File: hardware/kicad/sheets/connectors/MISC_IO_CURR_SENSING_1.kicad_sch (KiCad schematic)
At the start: 20 parts

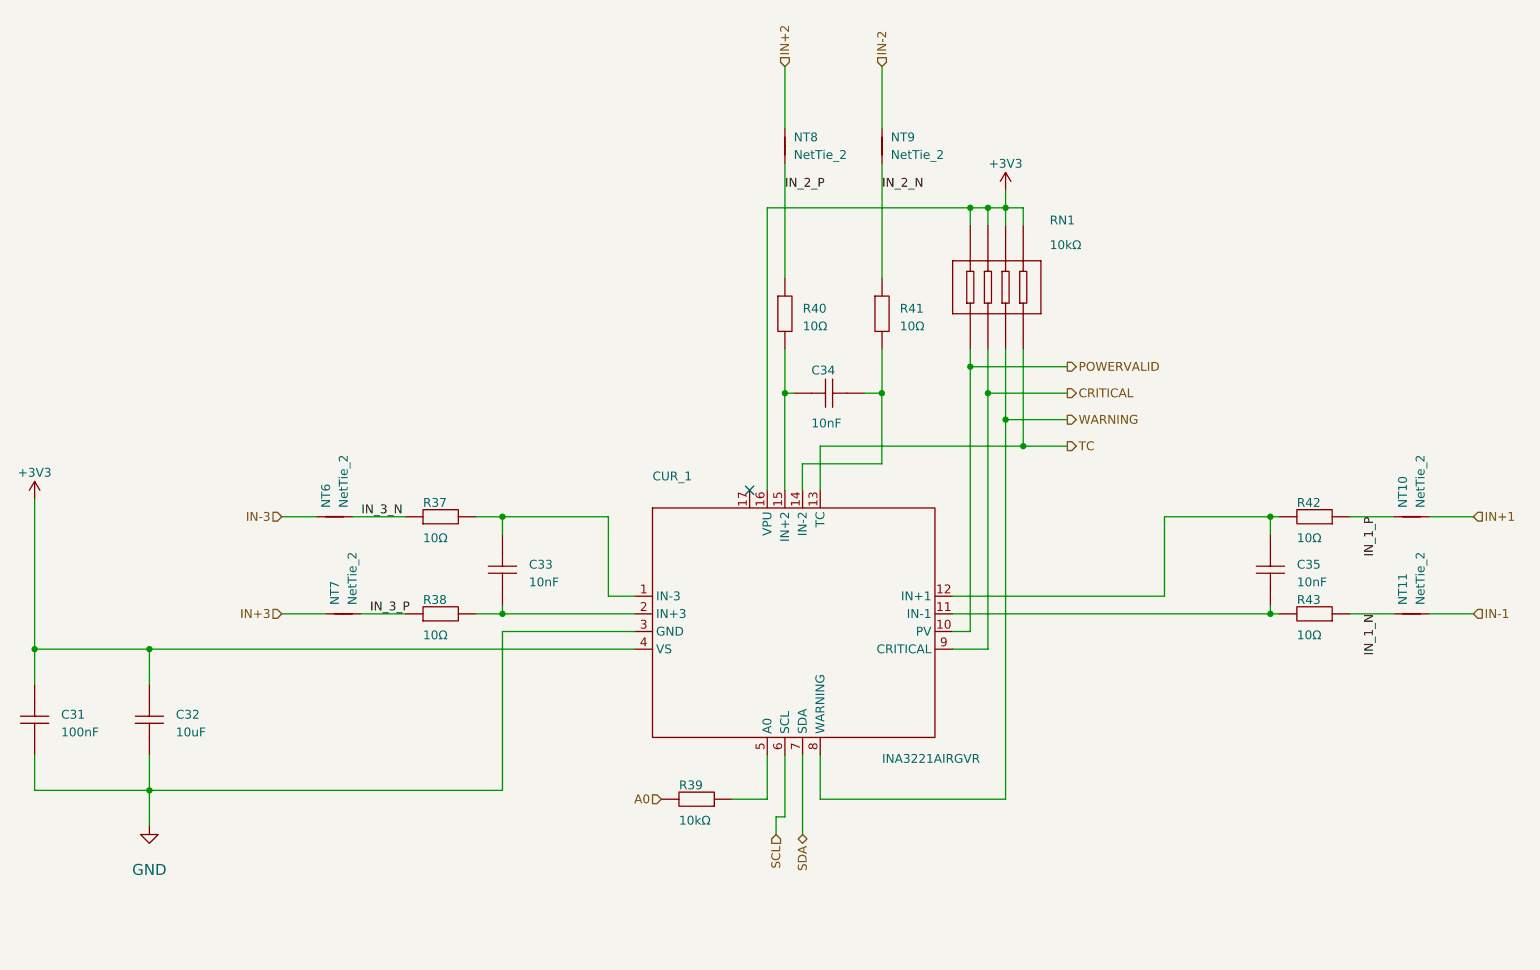
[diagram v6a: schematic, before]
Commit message: current sensing on the servos and cleaning up empty sheets
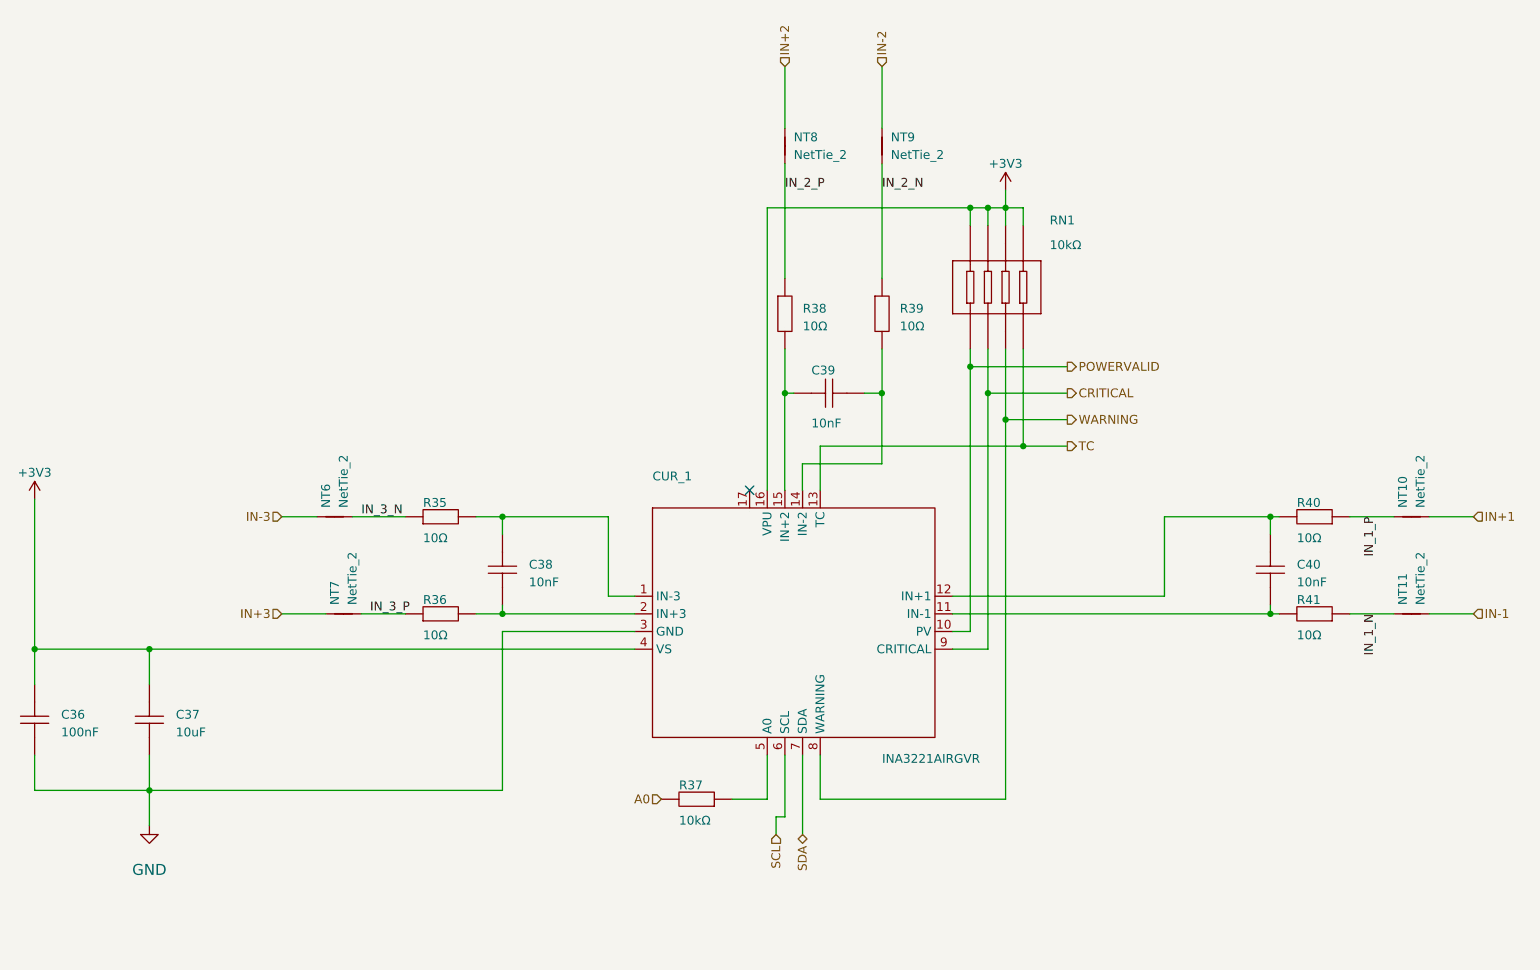
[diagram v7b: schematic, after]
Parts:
- renumbered C31 to C36, C32 to C37, C33 to C38, C34 to C39, C35 to C40, R37 to R35, R38 to R36, R39 to R37, R40 to R38, R41 to R39, R42 to R40, R43 to R41
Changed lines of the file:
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@@
 		(on_board yes)
 		(dnp no)
-		(property "Reference" "#PWR059"
+		(property "Reference" "#PWR060"
 			(at 63.5 142.24 0)
 			(effects
@@
 			(project "svea_powerboard_rev3"
 				(path "/3f85abf4-0b95-4c4a-b7e9-06f59ca1ea3d/5c2e021f-c2d4-49e2-8c36-9a64f1f12001/018d0221-df9b-4023-93f4-3996394924d7"
-					(reference "#PWR0149")
+					(reference "#PWR0151")
 					(unit 1)
 				)
 				(path "/3f85abf4-0b95-4c4a-b7e9-06f59ca1ea3d/5c2e021f-c2d4-49e2-8c36-9a64f1f12001/3defe835-7f3e-4186-81ed-0e8caa47e3eb"
-					(reference "#PWR059")
+					(reference "#PWR060")
 					(unit 1)
 				)
@@
 		(on_board yes)
 		(dnp no)
-		(property "Reference" "C33"
+		(property "Reference" "C38"
 			(at 118.11 105.41 90)
 			(effects
@@
 			(project "svea_powerboard_rev3"
 				(path "/3f85abf4-0b95-4c4a-b7e9-06f59ca1ea3d/5c2e021f-c2d4-49e2-8c36-9a64f1f12001/018d0221-df9b-4023-93f4-3996394924d7"
-					(reference "C97")
+					(reference "C102")
 					(unit 1)
 				)
 				(path "/3f85abf4-0b95-4c4a-b7e9-06f59ca1ea3d/5c2e021f-c2d4-49e2-8c36-9a64f1f12001/3defe835-7f3e-4186-81ed-0e8caa47e3eb"
-					(reference "C33")
+					(reference "C38")
 					(unit 1)
 				)
@@
 		(on_board yes)
 		(dnp no)
-		(property "Reference" "R43"
+		(property "Reference" "R41"
 			(at 228.6 110.49 0)
 			(effects
@@
 			(project "svea_powerboard_rev3"
 				(path "/3f85abf4-0b95-4c4a-b7e9-06f59ca1ea3d/5c2e021f-c2d4-49e2-8c36-9a64f1f12001/018d0221-df9b-4023-93f4-3996394924d7"
-					(reference "R109")
+					(reference "R106")
 					(unit 1)
 				)
 				(path "/3f85abf4-0b95-4c4a-b7e9-06f59ca1ea3d/5c2e021f-c2d4-49e2-8c36-9a64f1f12001/3defe835-7f3e-4186-81ed-0e8caa47e3eb"
-					(reference "R43")
+					(reference "R41")
 					(unit 1)
 				)
@@
 		(on_board yes)
 		(dnp no)
-		(property "Reference" "R39"
+		(property "Reference" "R37"
 			(at 139.7 137.16 0)
 			(effects
@@
 			(project "svea_powerboard_rev3"
 				(path "/3f85abf4-0b95-4c4a-b7e9-06f59ca1ea3d/5c2e021f-c2d4-49e2-8c36-9a64f1f12001/018d0221-df9b-4023-93f4-3996394924d7"
-					(reference "R105")
+					(reference "R102")
 					(unit 1)
 				)
 				(path "/3f85abf4-0b95-4c4a-b7e9-06f59ca1ea3d/5c2e021f-c2d4-49e2-8c36-9a64f1f12001/3defe835-7f3e-4186-81ed-0e8caa47e3eb"
-					(reference "R39")
+					(reference "R37")
 					(unit 1)
 				)
@@
 		(on_board yes)
 		(dnp no)
-		(property "Reference" "R41"
+		(property "Reference" "R39"
 			(at 171.4754 68.58 90)
 			(effects
@@
 			(project "svea_powerboard_rev3"
 				(path "/3f85abf4-0b95-4c4a-b7e9-06f59ca1ea3d/5c2e021f-c2d4-49e2-8c36-9a64f1f12001/018d0221-df9b-4023-93f4-3996394924d7"
-					(reference "R107")
+					(reference "R104")
 					(unit 1)
 				)
 				(path "/3f85abf4-0b95-4c4a-b7e9-06f59ca1ea3d/5c2e021f-c2d4-49e2-8c36-9a64f1f12001/3defe835-7f3e-4186-81ed-0e8caa47e3eb"
-					(reference "R41")
+					(reference "R39")
 					(unit 1)
 				)
@@
 		(on_board yes)
 		(dnp no)
-		(property "Reference" "C34"
+		(property "Reference" "C39"
 			(at 158.75 77.47 0)
 			(effects
@@
 			(project "svea_powerboard_rev3"
 				(path "/3f85abf4-0b95-4c4a-b7e9-06f59ca1ea3d/5c2e021f-c2d4-49e2-8c36-9a64f1f12001/018d0221-df9b-4023-93f4-3996394924d7"
-					(reference "C98")
+					(reference "C103")
 					(unit 1)
 				)
 				(path "/3f85abf4-0b95-4c4a-b7e9-06f59ca1ea3d/5c2e021f-c2d4-49e2-8c36-9a64f1f12001/3defe835-7f3e-4186-81ed-0e8caa47e3eb"
-					(reference "C34")
+					(reference "C39")
 					(unit 1)
 				)
@@
 		(on_board yes)
 		(dnp no)
-		(property "Reference" "C32"
+		(property "Reference" "C37"
 			(at 67.31 127 90)
 			(effects
@@
 			(project "svea_powerboard_rev3"
 				(path "/3f85abf4-0b95-4c4a-b7e9-06f59ca1ea3d/5c2e021f-c2d4-49e2-8c36-9a64f1f12001/018d0221-df9b-4023-93f4-3996394924d7"
-					(reference "C96")
+					(reference "C101")
 					(unit 1)
 				)
 				(path "/3f85abf4-0b95-4c4a-b7e9-06f59ca1ea3d/5c2e021f-c2d4-49e2-8c36-9a64f1f12001/3defe835-7f3e-4186-81ed-0e8caa47e3eb"
-					(reference "C32")
+					(reference "C37")
 					(unit 1)
 				)
@@
 		(on_board yes)
 		(dnp no)
-		(property "Reference" "#PWR060"
+		(property "Reference" "#PWR061"
 			(at 186.69 50.8 0)
 			(effects
@@
 			(project "svea_powerboard_rev3"
 				(path "/3f85abf4-0b95-4c4a-b7e9-06f59ca1ea3d/5c2e021f-c2d4-49e2-8c36-9a64f1f12001/018d0221-df9b-4023-93f4-3996394924d7"
-					(reference "#PWR0150")
+					(reference "#PWR0152")
 					(unit 1)
 				)
 				(path "/3f85abf4-0b95-4c4a-b7e9-06f59ca1ea3d/5c2e021f-c2d4-49e2-8c36-9a64f1f12001/3defe835-7f3e-4186-81ed-0e8caa47e3eb"
-					(reference "#PWR060")
+					(reference "#PWR061")
 					(unit 1)
 				)
@@
 		(on_board yes)
 		(dnp no)
-		(property "Reference" "#PWR058"
+		(property "Reference" "#PWR059"
 			(at 46.99 95.25 0)
 			(effects
@@
 			(project "svea_powerboard_rev3"
 				(path "/3f85abf4-0b95-4c4a-b7e9-06f59ca1ea3d/5c2e021f-c2d4-49e2-8c36-9a64f1f12001/018d0221-df9b-4023-93f4-3996394924d7"
-					(reference "#PWR0148")
+					(reference "#PWR0150")
 					(unit 1)
 				)
 				(path "/3f85abf4-0b95-4c4a-b7e9-06f59ca1ea3d/5c2e021f-c2d4-49e2-8c36-9a64f1f12001/3defe835-7f3e-4186-81ed-0e8caa47e3eb"
-					(reference "#PWR058")
+					(reference "#PWR059")
 					(unit 1)
 				)
@@
 		(on_board yes)
 		(dnp no)
-		(property "Reference" "R38"
+		(property "Reference" "R36"
 			(at 102.87 110.49 0)
 			(effects
@@
 			(project "svea_powerboard_rev3"
 				(path "/3f85abf4-0b95-4c4a-b7e9-06f59ca1ea3d/5c2e021f-c2d4-49e2-8c36-9a64f1f12001/018d0221-df9b-4023-93f4-3996394924d7"
-					(reference "R104")
+					(reference "R101")
 					(unit 1)
 				)
 				(path "/3f85abf4-0b95-4c4a-b7e9-06f59ca1ea3d/5c2e021f-c2d4-49e2-8c36-9a64f1f12001/3defe835-7f3e-4186-81ed-0e8caa47e3eb"
-					(reference "R38")
+					(reference "R36")
 					(unit 1)
 				)
@@
 		(on_board yes)
 		(dnp no)
-		(property "Reference" "R40"
+		(property "Reference" "R38"
 			(at 157.5054 68.58 90)
 			(effects
@@
 			(project "svea_powerboard_rev3"
 				(path "/3f85abf4-0b95-4c4a-b7e9-06f59ca1ea3d/5c2e021f-c2d4-49e2-8c36-9a64f1f12001/018d0221-df9b-4023-93f4-3996394924d7"
-					(reference "R106")
+					(reference "R103")
 					(unit 1)
 				)
 				(path "/3f85abf4-0b95-4c4a-b7e9-06f59ca1ea3d/5c2e021f-c2d4-49e2-8c36-9a64f1f12001/3defe835-7f3e-4186-81ed-0e8caa47e3eb"
-					(reference "R40")
+					(reference "R38")
 					(unit 1)
 				)
@@
 		(on_board yes)
 		(dnp no)
-		(property "Reference" "C31"
+		(property "Reference" "C36"
 			(at 50.8 127 90)
 			(effects
@@
 			(project "svea_powerboard_rev3"
 				(path "/3f85abf4-0b95-4c4a-b7e9-06f59ca1ea3d/5c2e021f-c2d4-49e2-8c36-9a64f1f12001/018d0221-df9b-4023-93f4-3996394924d7"
-					(reference "C95")
+					(reference "C100")
 					(unit 1)
 				)
 				(path "/3f85abf4-0b95-4c4a-b7e9-06f59ca1ea3d/5c2e021f-c2d4-49e2-8c36-9a64f1f12001/3defe835-7f3e-4186-81ed-0e8caa47e3eb"
-					(reference "C31")
+					(reference "C36")
 					(unit 1)
 				)
@@
 		(on_board yes)
 		(dnp no)
-		(property "Reference" "R42"
+		(property "Reference" "R40"
 			(at 228.6 96.52 0)
 			(effects
@@
 			(project "svea_powerboard_rev3"
 				(path "/3f85abf4-0b95-4c4a-b7e9-06f59ca1ea3d/5c2e021f-c2d4-49e2-8c36-9a64f1f12001/018d0221-df9b-4023-93f4-3996394924d7"
-					(reference "R108")
+					(reference "R105")
 					(unit 1)
 				)
 				(path "/3f85abf4-0b95-4c4a-b7e9-06f59ca1ea3d/5c2e021f-c2d4-49e2-8c36-9a64f1f12001/3defe835-7f3e-4186-81ed-0e8caa47e3eb"
-					(reference "R42")
+					(reference "R40")
 					(unit 1)
 				)
@@
 		(on_board yes)
 		(dnp no)
-		(property "Reference" "R37"
+		(property "Reference" "R35"
 			(at 102.87 96.52 0)
 			(effects
@@
 			(project "svea_powerboard_rev3"
 				(path "/3f85abf4-0b95-4c4a-b7e9-06f59ca1ea3d/5c2e021f-c2d4-49e2-8c36-9a64f1f12001/018d0221-df9b-4023-93f4-3996394924d7"
-					(reference "R103")
+					(reference "R100")
 					(unit 1)
 				)
 				(path "/3f85abf4-0b95-4c4a-b7e9-06f59ca1ea3d/5c2e021f-c2d4-49e2-8c36-9a64f1f12001/3defe835-7f3e-4186-81ed-0e8caa47e3eb"
-					(reference "R37")
+					(reference "R35")
 					(unit 1)
 				)
@@
 		(on_board yes)
 		(dnp no)
-		(property "Reference" "C35"
+		(property "Reference" "C40"
 			(at 228.6 105.41 90)
 			(effects
@@
 			(project "svea_powerboard_rev3"
 				(path "/3f85abf4-0b95-4c4a-b7e9-06f59ca1ea3d/5c2e021f-c2d4-49e2-8c36-9a64f1f12001/018d0221-df9b-4023-93f4-3996394924d7"
-					(reference "C99")
+					(reference "C104")
 					(unit 1)
 				)
 				(path "/3f85abf4-0b95-4c4a-b7e9-06f59ca1ea3d/5c2e021f-c2d4-49e2-8c36-9a64f1f12001/3defe835-7f3e-4186-81ed-0e8caa47e3eb"
-					(reference "C35")
-					(unit 1)
-				)
+					(reference "C40")
+					(unit 1)
+				)
